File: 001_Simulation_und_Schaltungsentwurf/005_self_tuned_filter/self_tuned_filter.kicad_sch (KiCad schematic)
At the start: 26 parts, among them IC1 MPY634KP, IC2 MPY634KP, IC4 MPY634KP, U1 TL082, U2 TL082, U3 TL082

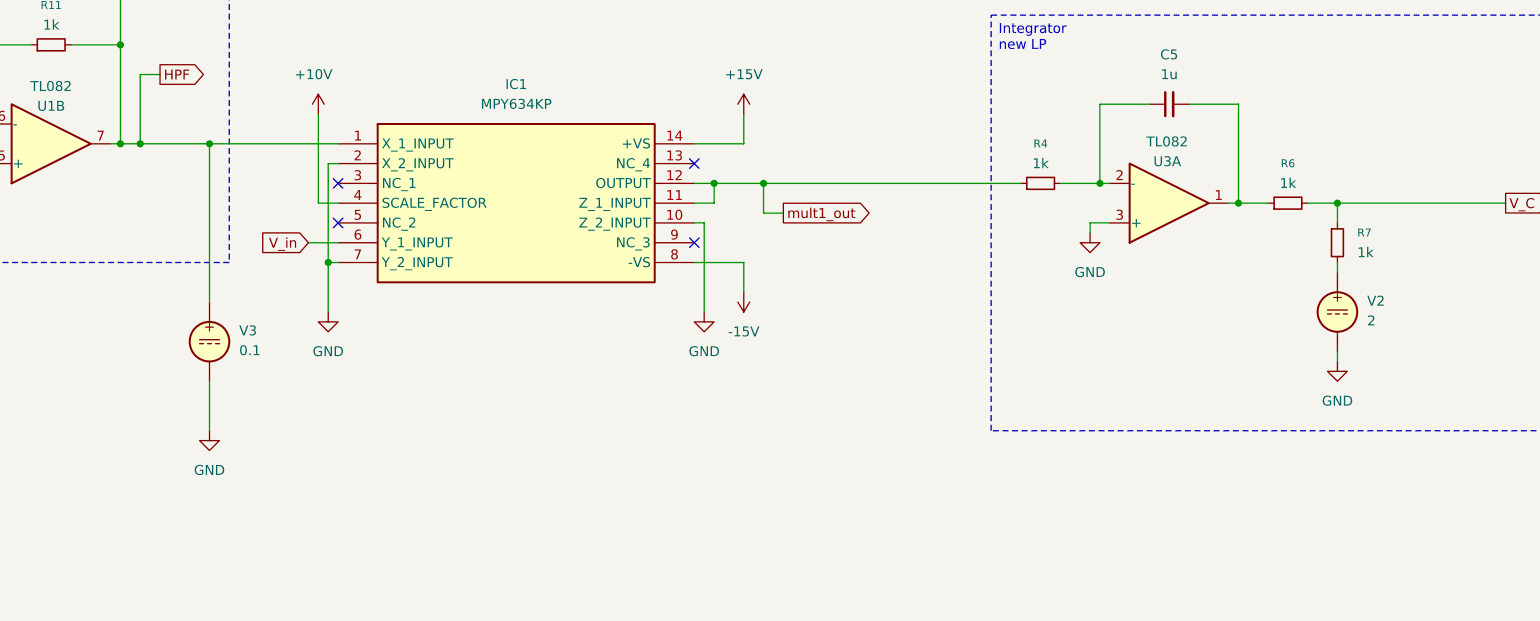
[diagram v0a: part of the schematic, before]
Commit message: Bestätigung der Gleichung für omega_0
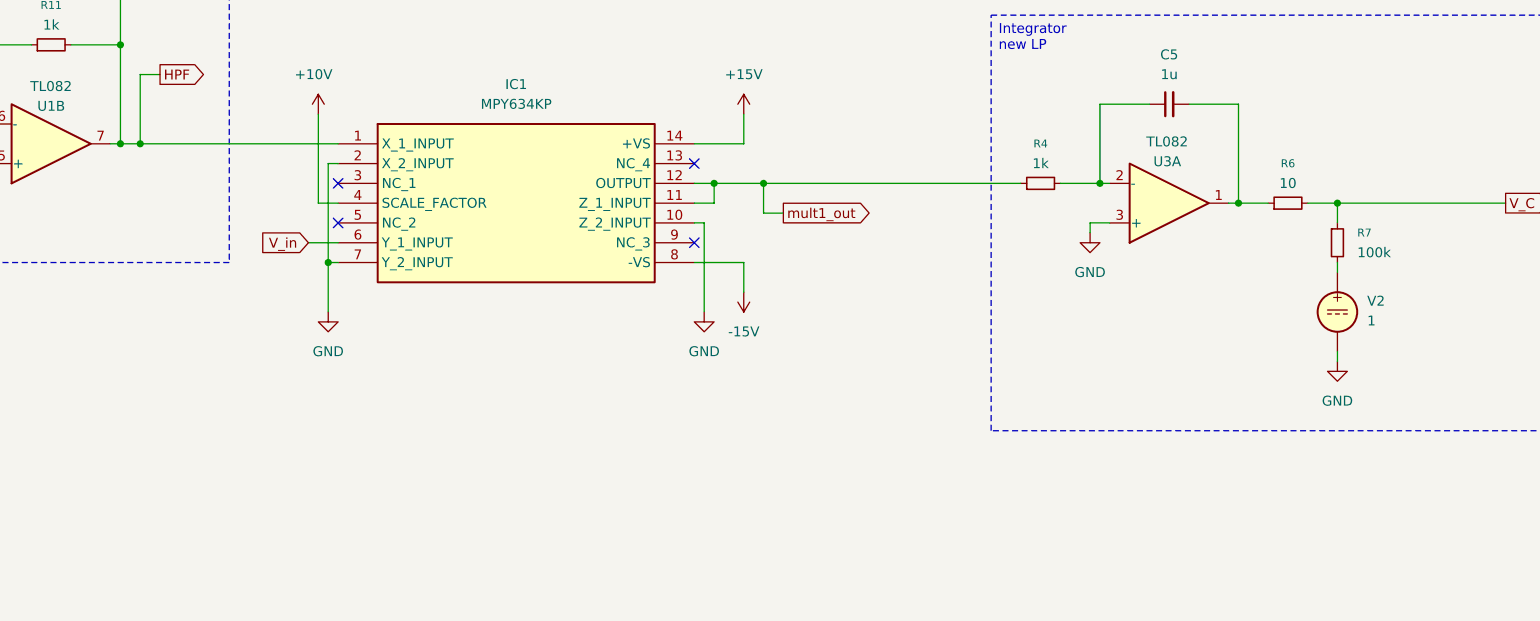
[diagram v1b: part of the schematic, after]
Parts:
- removed V3: 0.1, symbol Simulation_SPICE:VDC
- R6: value 1k -> 10
- R7: value 1k -> 100k
- V2: value 2 -> 1
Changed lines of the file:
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@@
 	)
 	(junction
-		(at 228.6 59.69)
-		(diameter 0)
-		(color 0 0 0 0)
-	)
-	(junction
 		(at 43.18 148.59)
 		(diameter 0)
@@
 	(wire
 		(pts
-			(xy 228.6 59.69) (xy 228.6 80.01)
-		)
-		(stroke
-			(width 0)
-			(type default)
-		)
-	)
-	(wire
-		(pts
 			(xy 297.18 55.88) (xy 297.18 59.69)
 		)
@@
 	(wire
 		(pts
-			(xy 219.71 59.69) (xy 228.6 59.69)
+			(xy 219.71 59.69) (xy 245.11 59.69)
 		)
 		(stroke
@@
 	(wire
 		(pts
-			(xy 228.6 90.17) (xy 228.6 96.52)
-		)
-		(stroke
-			(width 0)
-			(type default)
-		)
-	)
-	(wire
-		(pts
 			(xy 186.69 149.86) (xy 187.96 149.86)
 		)
@@
 	(wire
 		(pts
-			(xy 228.6 59.69) (xy 245.11 59.69)
-		)
-		(stroke
-			(width 0)
-			(type default)
-		)
-	)
-	(wire
-		(pts
 			(xy 360.68 67.31) (xy 364.49 67.31)
 		)
@@
 			)
 		)
-		(property "Value" "2"
+		(property "Value" "1"
 			(at 377.19 82.4201 0)
 			(effects
@@
 	)
 	(symbol
-		(lib_id "Simulation_SPICE:VDC")
-		(at 228.6 85.09 0)
-		(unit 1)
-		(exclude_from_sim no)
-		(in_bom yes)
-		(on_board yes)
-		(dnp no)
-		(fields_autoplaced yes)
-		(property "Reference" "V3"
-			(at 232.41 83.6901 0)
-			(effects
-				(font
-					(size 1.27 1.27)
-				)
-				(justify left)
-			)
-		)
-		(property "Value" "0.1"
-			(at 232.41 86.2301 0)
-			(effects
-				(font
-					(size 1.27 1.27)
-				)
-				(justify left)
-			)
-		)
-		(property "Footprint" ""
-			(at 228.6 85.09 0)
-			(effects
-				(font
-					(size 1.27 1.27)
-				)
-				(hide yes)
-			)
-		)
-		(property "Datasheet" "https://ngspice.sourceforge.io/docs/ngspice-html-manual/manual.xhtml#sec_Independent_Sources_for"
-			(at 228.6 85.09 0)
-			(effects
-				(font
-					(size 1.27 1.27)
-				)
-				(hide yes)
-			)
-		)
-		(property "Description" "Voltage source, DC"
-			(at 228.6 85.09 0)
-			(effects
-				(font
-					(size 1.27 1.27)
-				)
-				(hide yes)
-			)
-		)
-		(property "Sim.Pins" "1=+ 2=-"
-			(at 228.6 85.09 0)
-			(effects
-				(font
-					(size 1.27 1.27)
-				)
-				(hide yes)
-			)
-		)
-		(property "Sim.Type" "DC"
-			(at 228.6 85.09 0)
-			(effects
-				(font
-					(size 1.27 1.27)
-				)
-				(hide yes)
-			)
-		)
-		(property "Sim.Device" "V"
-			(at 228.6 85.09 0)
-			(effects
-				(font
-					(size 1.27 1.27)
-				)
-				(justify left)
-				(hide yes)
-			)
-		)
-		(pin "2"
-		)
-		(pin "1"
-		)
-		(instances
-			(project "selfe_tuned_filter"
-				(path "/8c03fc9a-cf6b-4365-99d8-e11c100e5159"
-					(reference "V3")
-					(unit 1)
-				)
-			)
-		)
-	)
-	(symbol
 		(lib_id "Device:C_Small")
 		(at 135.89 48.26 90)
@@
 			)
 		)
-		(property "Value" "1k"
+		(property "Value" "10"
 			(at 367.03 64.77 90)
 			(effects
@@
 	)
 	(symbol
-		(lib_id "power:GND")
-		(at 228.6 96.52 0)
-		(unit 1)
-		(exclude_from_sim no)
-		(in_bom yes)
-		(on_board yes)
-		(dnp no)
-		(fields_autoplaced yes)
-		(property "Reference" "#PWR013"
-			(at 228.6 102.87 0)
-			(effects
-				(font
-					(size 1.27 1.27)
-				)
-				(hide yes)
-			)
-		)
-		(property "Value" "GND"
-			(at 228.6 101.6 0)
-			(effects
-				(font
-					(size 1.27 1.27)
-				)
-			)
-		)
-		(property "Footprint" ""
-			(at 228.6 96.52 0)
-			(effects
-				(font
-					(size 1.27 1.27)
-				)
-				(hide yes)
-			)
-		)
-		(property "Datasheet" ""
-			(at 228.6 96.52 0)
-			(effects
-				(font
-					(size 1.27 1.27)
-				)
-				(hide yes)
-			)
-		)
-		(property "Description" "Power symbol creates a global label with name \"GND\" , ground"
-			(at 228.6 96.52 0)
-			(effects
-				(font
-					(size 1.27 1.27)
-				)
-				(hide yes)
-			)
-		)
-		(pin "1"
-		)
-		(instances
-			(project "selfe_tuned_filter"
-				(path "/8c03fc9a-cf6b-4365-99d8-e11c100e5159"
-					(reference "#PWR013")
-					(unit 1)
-				)
-			)
-		)
-	)
-	(symbol
 		(lib_id "Device:R_Small")
 		(at 184.15 64.77 90)
@@
 			)
 		)
-		(property "Value" "1k"
+		(property "Value" "100k"
 			(at 375.92 73.6599 0)
 			(effects
